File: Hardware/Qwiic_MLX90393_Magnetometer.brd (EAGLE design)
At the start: 25.4 x 25.4 mm, 24 parts

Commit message: post qc checklist changes
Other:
- board text added: "R. Reynolds"
- board text added: "Units in inches"
- board text added: "v10"
- board text removed: "J. Bartlett"
- board text removed: "v01"
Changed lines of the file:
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@@
 <text x="22.86" y="14.732" size="1.016" layer="21" font="vector" ratio="15" align="bottom-right">INT</text>
 <text x="22.86" y="17.272" size="1.016" layer="21" font="vector" ratio="15" align="bottom-right">TRIG</text>
-<text x="10.16" y="-10.16" size="1.778" layer="51" font="vector">J. Bartlett</text>
+<text x="10.16" y="-10.16" size="1.778" layer="51" font="vector">R. Reynolds</text>
 <text x="4.191" y="17.272" size="1.016" layer="22" font="vector" ratio="15" rot="MR0">CS</text>
 <text x="5.715" y="14.732" size="1.016" layer="22" font="vector" ratio="15" rot="MR0">MISO</text>
@@
 <text x="12.7" y="7.62" size="1.27" layer="22" font="vector" ratio="15" rot="MR0" align="bottom-center">Qwiic
 MLX90393</text>
-<text x="25.019" y="0.381" size="1.27" layer="16" font="vector" ratio="15" rot="MR0">v01</text>
+<text x="25.019" y="0.381" size="1.27" layer="16" font="vector" ratio="15" rot="MR0">v10</text>
 <dimension x1="0" y1="0" x2="0" y2="25.4" x3="-1.27" y3="12.7" textsize="1.778" textratio="15" layer="47" unit="inch"/>
 <dimension x1="2.54" y1="22.86" x2="2.54" y2="0" x3="-5.08" y3="11.43" textsize="1.778" textratio="15" layer="47" unit="inch"/>
@@
 <dimension x1="25.4" y1="25.4" x2="0" y2="25.4" x3="12.7" y3="30.48" textsize="1.778" textratio="15" layer="47" dtype="horizontal" unit="inch"/>
 <text x="10.16" y="-12.7" size="1.778" layer="51" font="vector">A. England</text>
+<text x="1.27" y="34.29" size="1.778" layer="47" font="vector">Units in inches</text>
 </plain>
 <attributes>

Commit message: fixed version number
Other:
- board text added: "v01"
- board text removed: "v10"
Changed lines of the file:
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@@
 <layer number="20" name="Dimension" color="15" fill="1" visible="yes" active="yes"/>
 <layer number="21" name="tPlace" color="16" fill="1" visible="yes" active="yes"/>
-<layer number="22" name="bPlace" color="14" fill="1" visible="yes" active="yes"/>
+<layer number="22" name="bPlace" color="14" fill="1" visible="no" active="yes"/>
 <layer number="23" name="tOrigins" color="15" fill="1" visible="yes" active="yes"/>
-<layer number="24" name="bOrigins" color="15" fill="1" visible="yes" active="yes"/>
-<layer number="25" name="tNames" color="7" fill="1" visible="no" active="yes"/>
+<layer number="24" name="bOrigins" color="15" fill="1" visible="no" active="yes"/>
+<layer number="25" name="tNames" color="7" fill="1" visible="yes" active="yes"/>
 <layer number="26" name="bNames" color="7" fill="1" visible="no" active="yes"/>
 <layer number="27" name="tValues" color="7" fill="1" visible="no" active="yes"/>
@@
 <layer number="37" name="tTest" color="7" fill="1" visible="no" active="yes"/>
 <layer number="38" name="bTest" color="7" fill="1" visible="no" active="yes"/>
-<layer number="39" name="tKeepout" color="4" fill="11" visible="yes" active="yes"/>
-<layer number="40" name="bKeepout" color="1" fill="11" visible="yes" active="yes"/>
+<layer number="39" name="tKeepout" color="4" fill="11" visible="no" active="yes"/>
+<layer number="40" name="bKeepout" color="1" fill="11" visible="no" active="yes"/>
 <layer number="41" name="tRestrict" color="4" fill="10" visible="no" active="yes"/>
 <layer number="42" name="bRestrict" color="1" fill="10" visible="no" active="yes"/>
 <layer number="43" name="vRestrict" color="2" fill="10" visible="no" active="yes"/>
 <layer number="44" name="Drills" color="7" fill="1" visible="no" active="yes"/>
-<layer number="45" name="Holes" color="7" fill="1" visible="yes" active="yes"/>
+<layer number="45" name="Holes" color="7" fill="1" visible="no" active="yes"/>
 <layer number="46" name="Milling" color="3" fill="1" visible="no" active="yes"/>
-<layer number="47" name="Measures" color="7" fill="1" visible="yes" active="yes"/>
+<layer number="47" name="Measures" color="7" fill="1" visible="no" active="yes"/>
 <layer number="48" name="Document" color="7" fill="1" visible="no" active="yes"/>
-<layer number="49" name="Reference" color="7" fill="1" visible="yes" active="yes"/>
+<layer number="49" name="Reference" color="7" fill="1" visible="no" active="yes"/>
 <layer number="50" name="dxf" color="7" fill="1" visible="no" active="no"/>
-<layer number="51" name="tDocu" color="6" fill="1" visible="yes" active="yes"/>
+<layer number="51" name="tDocu" color="6" fill="1" visible="no" active="yes"/>
 <layer number="52" name="bDocu" color="7" fill="1" visible="no" active="yes"/>
 <layer number="53" name="tGND_GNDA" color="7" fill="9" visible="no" active="no"/>
@@
 <text x="12.7" y="7.62" size="1.27" layer="22" font="vector" ratio="15" rot="MR0" align="bottom-center">Qwiic
 MLX90393</text>
-<text x="25.019" y="0.381" size="1.27" layer="16" font="vector" ratio="15" rot="MR0">v10</text>
+<text x="25.019" y="0.381" size="1.27" layer="16" font="vector" ratio="15" rot="MR0">v01</text>
 <dimension x1="0" y1="0" x2="0" y2="25.4" x3="-1.27" y3="12.7" textsize="1.778" textratio="15" layer="47" unit="inch"/>
 <dimension x1="2.54" y1="22.86" x2="2.54" y2="0" x3="-5.08" y3="11.43" textsize="1.778" textratio="15" layer="47" unit="inch"/>

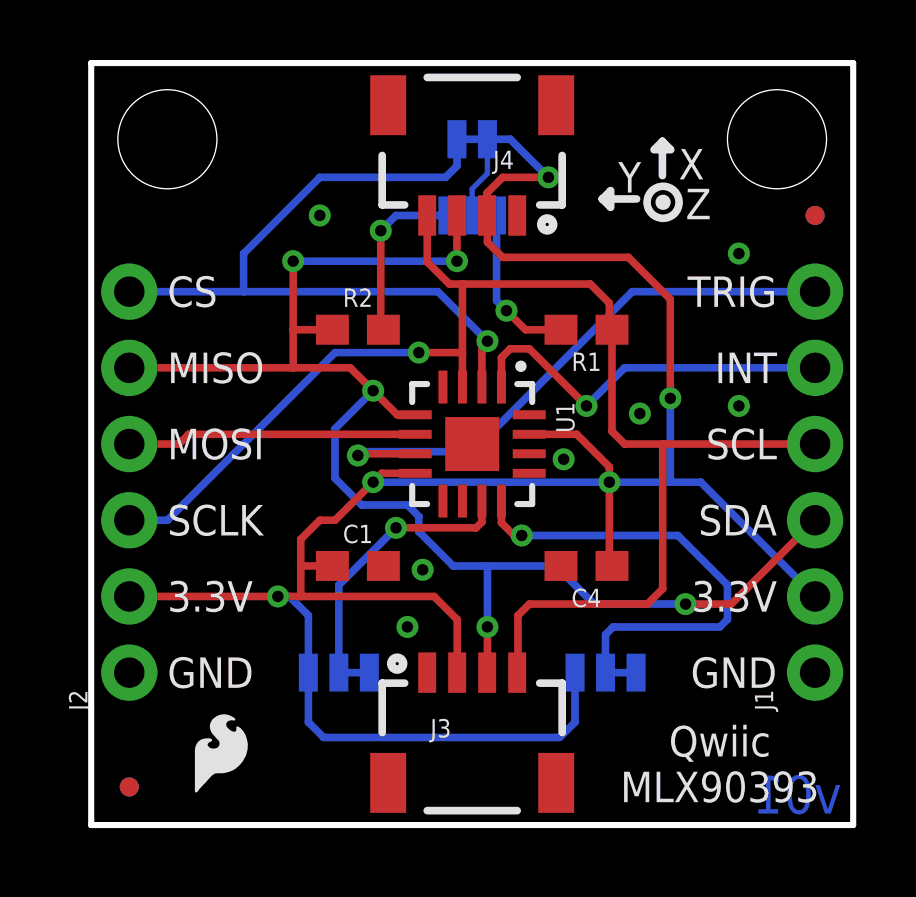
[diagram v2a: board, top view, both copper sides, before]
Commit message: updated footprint for magnetometer
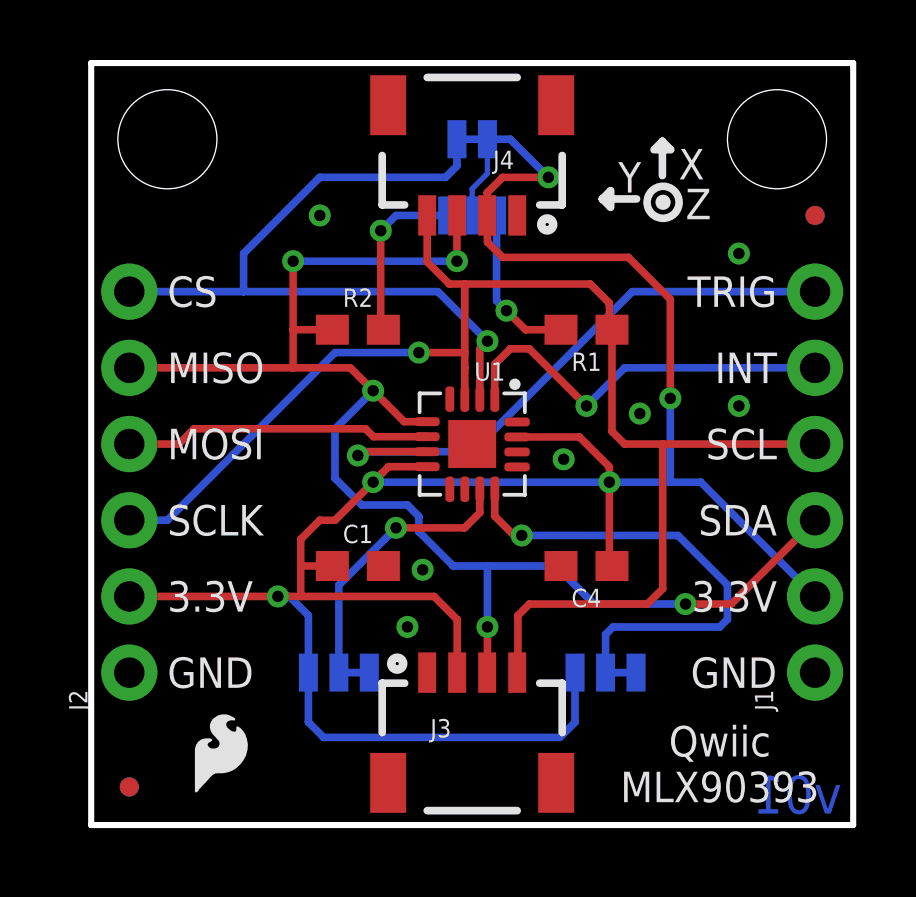
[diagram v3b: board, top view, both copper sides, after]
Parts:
- U1: value (none) -> MLX90393_MAGNETOMETER; device SparkFun-Sensors:HVQFN-16 -> SparkFun-Sensors:QFN-16_WITH_AXIES
- turned U1 to 0 degrees
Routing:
- net 3.3V: track 81.6 -> 82.9 mm
- net CS: track 24.7 -> 25.4 mm
- net MISO: track 9.66 -> 10.2 mm
- net TRIG: track 19.4 -> 19.9 mm
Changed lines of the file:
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@@
 </autorouter>
 <elements>
-<element name="U1" library="SparkFun-Sensors" package="HVQFN-16" value="" x="12.7" y="12.7" rot="R270">
-<attribute name="PROD_ID" value="SEN-13886" x="12.7" y="12.7" size="1.778" layer="27" rot="R270" display="off"/>
-<attribute name="VALUE" value="" x="12.7" y="12.7" size="1.778" layer="27" rot="R270" display="off"/>
+<element name="U1" library="SparkFun-Sensors" package="QFN-16_WITH_AXIES" value="MLX90393_MAGNETOMETER" x="12.7" y="12.7">
+<attribute name="PROD_ID" value="SEN-13886" x="12.7" y="12.7" size="1.778" layer="27" display="off"/>
 </element>
 <element name="R1" library="SparkFun-Resistors" package="0603" value="10k" x="16.51" y="16.51" rot="R180">
@@
 <wire x1="17.272" y1="16.598" x2="17.272" y2="17.399" width="0.254" layer="1"/>
 <wire x1="17.272" y1="17.399" x2="16.637" y2="18.034" width="0.254" layer="1"/>
-<wire x1="16.637" y1="18.034" x2="12.375" y2="18.034" width="0.254" layer="1"/>
-<wire x1="12.375" y1="18.034" x2="11.938" y2="18.034" width="0.254" layer="1"/>
+<wire x1="16.637" y1="18.034" x2="12.454" y2="18.034" width="0.254" layer="1"/>
+<wire x1="12.454" y1="18.034" x2="11.938" y2="18.034" width="0.254" layer="1"/>
 <wire x1="2.54" y1="10.16" x2="1.27" y2="10.16" width="0.254" layer="16"/>
 <wire x1="14.224" y1="6.985" x2="14.605" y2="7.366" width="0.254" layer="1"/>
@@
 <wire x1="11.2" y1="20.32" x2="11.2" y2="18.772" width="0.254" layer="1"/>
 <wire x1="11.2" y1="18.772" x2="11.938" y2="18.034" width="0.254" layer="1"/>
-<wire x1="12.375" y1="14.6" x2="12.375" y2="15.748" width="0.254" layer="1"/>
-<wire x1="12.375" y1="15.748" x2="12.375" y2="18.034" width="0.254" layer="1"/>
-<wire x1="10.922" y1="15.748" x2="12.375" y2="15.748" width="0.254" layer="1"/>
 <wire x1="8.128" y1="15.748" x2="2.54" y2="10.16" width="0.254" layer="16"/>
 <wire x1="10.922" y1="15.748" x2="8.128" y2="15.748" width="0.254" layer="16"/>
+<wire x1="12.454" y1="14.198" x2="12.454" y2="15.24" width="0.254" layer="1"/>
+<wire x1="12.454" y1="15.748" x2="12.454" y2="18.034" width="0.254" layer="1"/>
+<wire x1="10.922" y1="15.748" x2="12.454" y2="15.748" width="0.254" layer="1"/>
+<wire x1="12.454" y1="15.748" x2="12.454" y2="15.24" width="0.254" layer="1"/>
 </signal>
 <signal name="SDA">
@@
 <wire x1="9.398" y1="14.478" x2="8.636" y2="15.24" width="0.254" layer="1"/>
 <via x="9.398" y="14.478" extent="1-16" drill="0.381"/>
-<wire x1="10.8" y1="13.675" x2="10.201" y2="13.675" width="0.254" layer="1"/>
-<wire x1="10.201" y1="13.675" x2="9.398" y2="14.478" width="0.254" layer="1"/>
+<wire x1="10.43" y1="13.446" x2="9.398" y2="14.478" width="0.254" layer="1"/>
 <wire x1="10.922" y1="9.779" x2="10.922" y2="10.287" width="0.254" layer="16"/>
 <wire x1="10.922" y1="10.287" x2="10.541" y2="10.668" width="0.254" layer="16"/>
@@
 <wire x1="6.731" y1="16.51" x2="6.731" y2="15.24" width="0.254" layer="1"/>
 <wire x1="8.04" y1="16.51" x2="6.731" y2="16.51" width="0.254" layer="1"/>
+<wire x1="11.192" y1="13.446" x2="10.43" y2="13.446" width="0.254" layer="1"/>
 </signal>
 <signal name="CS">
@@
 <wire x1="12.192" y1="21.971" x2="11.811" y2="21.59" width="0.254" layer="16"/>
 <wire x1="13.208" y1="16.129" x2="13.025" y2="15.946" width="0.254" layer="1"/>
-<wire x1="13.025" y1="15.946" x2="13.025" y2="14.6" width="0.254" layer="1"/>
+<wire x1="12.954" y1="14.198" x2="12.954" y2="15.875" width="0.254" layer="1"/>
+<wire x1="12.954" y1="15.875" x2="13.208" y2="16.129" width="0.254" layer="1"/>
 </signal>
 <signal name="N$4">
@@
 <contactref element="U1" pad="6"/>
 <contactref element="J2" pad="4"/>
-<wire x1="3.246" y1="13.025" x2="2.921" y2="12.7" width="0.254" layer="1"/>
 <wire x1="2.921" y1="12.7" x2="1.27" y2="12.7" width="0.254" layer="1"/>
-<wire x1="3.246" y1="13.025" x2="10.8" y2="13.025" width="0.254" layer="1"/>
+<wire x1="11.192" y1="12.946" x2="9.406" y2="12.946" width="0.254" layer="1"/>
+<wire x1="9.406" y1="12.946" x2="9.144" y2="13.208" width="0.254" layer="1"/>
+<wire x1="9.144" y1="13.208" x2="3.429" y2="13.208" width="0.254" layer="1"/>
+<wire x1="3.429" y1="13.208" x2="2.921" y2="12.7" width="0.254" layer="1"/>
 </signal>
 <signal name="INT">
@@
 <wire x1="24.13" y1="15.24" x2="17.78" y2="15.24" width="0.254" layer="16"/>
 <wire x1="17.78" y1="15.24" x2="16.51" y2="13.97" width="0.254" layer="16"/>
-<wire x1="13.675" y1="14.6" x2="13.675" y2="15.58" width="0.254" layer="1"/>
-<wire x1="13.675" y1="15.58" x2="13.97" y2="15.875" width="0.254" layer="1"/>
+<wire x1="13.454" y1="15.359" x2="13.97" y2="15.875" width="0.254" layer="1"/>
 <wire x1="13.97" y1="15.875" x2="14.605" y2="15.875" width="0.254" layer="1"/>
 <wire x1="14.605" y1="15.875" x2="16.51" y2="13.97" width="0.254" layer="1"/>
 <via x="16.51" y="13.97" extent="1-16" drill="0.381"/>
+<wire x1="13.454" y1="14.198" x2="13.454" y2="15.359" width="0.254" layer="1"/>
 </signal>
 <signal name="TRIG">
@@
 <wire x1="12.7" y1="12.446" x2="18.034" y2="17.78" width="0.254" layer="16"/>
 <wire x1="18.034" y1="17.78" x2="24.13" y2="17.78" width="0.254" layer="16"/>
-<wire x1="10.8" y1="12.375" x2="8.946" y2="12.375" width="0.254" layer="1"/>
 <via x="8.89" y="12.319" extent="1-16" drill="0.381"/>
 <wire x1="12.7" y1="12.446" x2="9.017" y2="12.446" width="0.254" layer="16"/>
 <wire x1="9.017" y1="12.446" x2="8.89" y2="12.319" width="0.254" layer="16"/>
 <wire x1="8.946" y1="12.375" x2="8.89" y2="12.319" width="0.254" layer="1"/>
+<wire x1="11.192" y1="12.446" x2="9.017" y2="12.446" width="0.254" layer="1"/>
+<wire x1="9.017" y1="12.446" x2="8.89" y2="12.319" width="0.254" layer="1"/>
 </signal>
 <signal name="A0">
@@
 <wire x1="20.955" y1="6.604" x2="21.209" y2="6.858" width="0.254" layer="16"/>
 <wire x1="21.209" y1="6.858" x2="21.209" y2="8.001" width="0.254" layer="16"/>
-<wire x1="13.675" y1="10.8" x2="13.675" y2="10.074" width="0.254" layer="1"/>
-<wire x1="13.675" y1="10.074" x2="14.097" y2="9.652" width="0.254" layer="1"/>
+<wire x1="13.454" y1="10.295" x2="14.097" y2="9.652" width="0.254" layer="1"/>
 <wire x1="14.097" y1="9.652" x2="14.351" y2="9.652" width="0.254" layer="1"/>
+<wire x1="13.454" y1="11.194" x2="13.454" y2="10.295" width="0.254" layer="1"/>
 </signal>
 <signal name="A1">
 <contactref element="U1" pad="11"/>
 <contactref element="SJ4" pad="2"/>
-<wire x1="12.827" y1="9.906" x2="10.16" y2="9.906" width="0.254" layer="1"/>
 <via x="10.16" y="9.906" extent="1-16" drill="0.381"/>
 <wire x1="10.16" y1="9.906" x2="8.255" y2="8.001" width="0.254" layer="16"/>
 <wire x1="8.255" y1="5.08" x2="8.255" y2="8.001" width="0.254" layer="16"/>
-<wire x1="12.827" y1="9.906" x2="13.025" y2="10.104" width="0.254" layer="1"/>
-<wire x1="13.025" y1="10.104" x2="13.025" y2="10.8" width="0.254" layer="1"/>
+<wire x1="12.954" y1="11.194" x2="12.954" y2="10.414" width="0.254" layer="1"/>
+<wire x1="12.954" y1="10.414" x2="12.446" y2="9.906" width="0.254" layer="1"/>
+<wire x1="12.446" y1="9.906" x2="10.16" y2="9.906" width="0.254" layer="1"/>
 </signal>
 <signal name="3.3V">
@@
 <wire x1="15.24" y1="21.59" x2="13.97" y2="22.86" width="0.254" layer="16"/>
 <wire x1="13.97" y1="22.86" x2="13.208" y2="22.86" width="0.254" layer="16"/>
-<wire x1="16.185" y1="13.025" x2="14.6" y2="13.025" width="0.254" layer="1"/>
 <wire x1="9.398" y1="11.43" x2="9.693" y2="11.725" width="0.254" layer="1"/>
-<wire x1="9.693" y1="11.725" x2="10.8" y2="11.725" width="0.254" layer="1"/>
 <wire x1="24.13" y1="7.62" x2="20.32" y2="11.43" width="0.254" layer="16"/>
 <wire x1="20.32" y1="11.43" x2="19.304" y2="11.43" width="0.254" layer="16"/>
@@
 <wire x1="19.304" y1="14.224" x2="19.304" y2="11.43" width="0.254" layer="16"/>
 <wire x1="17.272" y1="11.43" x2="17.272" y2="11.938" width="0.254" layer="1"/>
-<wire x1="17.272" y1="11.938" x2="16.185" y2="13.025" width="0.254" layer="1"/>
 <wire x1="17.272" y1="11.43" x2="17.272" y2="8.724" width="0.254" layer="1"/>
 <wire x1="17.272" y1="8.724" x2="17.36" y2="8.636" width="0.254" layer="1"/>
@@
 <wire x1="7.62" y1="10.16" x2="8.128" y2="10.16" width="0.254" layer="1"/>
 <wire x1="8.128" y1="10.16" x2="9.398" y2="11.43" width="0.254" layer="1"/>
+<wire x1="14.196" y1="12.936" x2="16.274" y2="12.936" width="0.254" layer="1"/>
+<wire x1="16.274" y1="12.936" x2="17.272" y2="11.938" width="0.254" layer="1"/>
+<wire x1="11.192" y1="11.946" x2="9.914" y2="11.946" width="0.254" layer="1"/>
+<wire x1="9.914" y1="11.946" x2="9.398" y2="11.43" width="0.254" layer="1"/>
 </signal>
 </signals>

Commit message: post checklist changes
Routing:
- net GND: track 0.98 -> 2.53 mm
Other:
- board text added: "0"
- board text added: "1"
- board text added: "v10"
- board text removed: "v01"
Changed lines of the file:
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@@
 <text x="12.7" y="7.62" size="1.27" layer="22" font="vector" ratio="15" rot="MR0" align="bottom-center">Qwiic
 MLX90393</text>
-<text x="25.019" y="0.381" size="1.27" layer="16" font="vector" ratio="15" rot="MR0">v01</text>
+<text x="25.019" y="0.381" size="1.27" layer="16" font="vector" ratio="15" rot="MR0">v10</text>
 <dimension x1="0" y1="0" x2="0" y2="25.4" x3="-1.27" y3="12.7" textsize="1.778" textratio="15" layer="47" unit="inch"/>
 <dimension x1="2.54" y1="22.86" x2="2.54" y2="0" x3="-5.08" y3="11.43" textsize="1.778" textratio="15" layer="47" unit="inch"/>
@@
 <text x="10.16" y="-12.7" size="1.778" layer="51" font="vector">A. England</text>
 <text x="1.27" y="34.29" size="1.778" layer="47" font="vector">Units in inches</text>
+<text x="18.034" y="3.302" size="1.016" layer="22" font="vector" ratio="15" rot="MR0" align="center">0</text>
+<text x="16.002" y="3.302" size="1.016" layer="22" font="vector" ratio="15" rot="MR0" align="center">1</text>
+<text x="9.144" y="3.302" size="1.016" layer="22" font="vector" ratio="15" rot="MR0" align="center">0</text>
+<text x="7.112" y="3.302" size="1.016" layer="22" font="vector" ratio="15" rot="MR0" align="center">1</text>
 </plain>
 <attributes>
@@
 <via x="21.59" y="19.05" extent="1-16" drill="0.381"/>
 <via x="7.62" y="20.32" extent="1-16" drill="0.381"/>
+<wire x1="14.196" y1="11.936" x2="15.24" y2="11.936" width="0.2032" layer="1"/>
+<wire x1="15.24" y1="11.936" x2="15.24" y2="11.43" width="0.2032" layer="1"/>
 </signal>
 <signal name="SCL">
@@
 <wire x1="8.128" y1="15.748" x2="2.54" y2="10.16" width="0.254" layer="16"/>
 <wire x1="10.922" y1="15.748" x2="8.128" y2="15.748" width="0.254" layer="16"/>
-<wire x1="12.454" y1="14.198" x2="12.454" y2="15.24" width="0.254" layer="1"/>
+<wire x1="12.454" y1="14.198" x2="12.454" y2="15.748" width="0.254" layer="1"/>
 <wire x1="12.454" y1="15.748" x2="12.454" y2="18.034" width="0.254" layer="1"/>
 <wire x1="10.922" y1="15.748" x2="12.454" y2="15.748" width="0.254" layer="1"/>
-<wire x1="12.454" y1="15.748" x2="12.454" y2="15.24" width="0.254" layer="1"/>
 </signal>
 <signal name="SDA">
